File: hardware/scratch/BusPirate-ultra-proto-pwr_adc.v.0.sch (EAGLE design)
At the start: 13 parts, among them IC1 IC_MCP1824_ADJ, Q1 DMMT3906W, Q2 DMMT3906W, U1 IC_OP-AMP_MCP6001

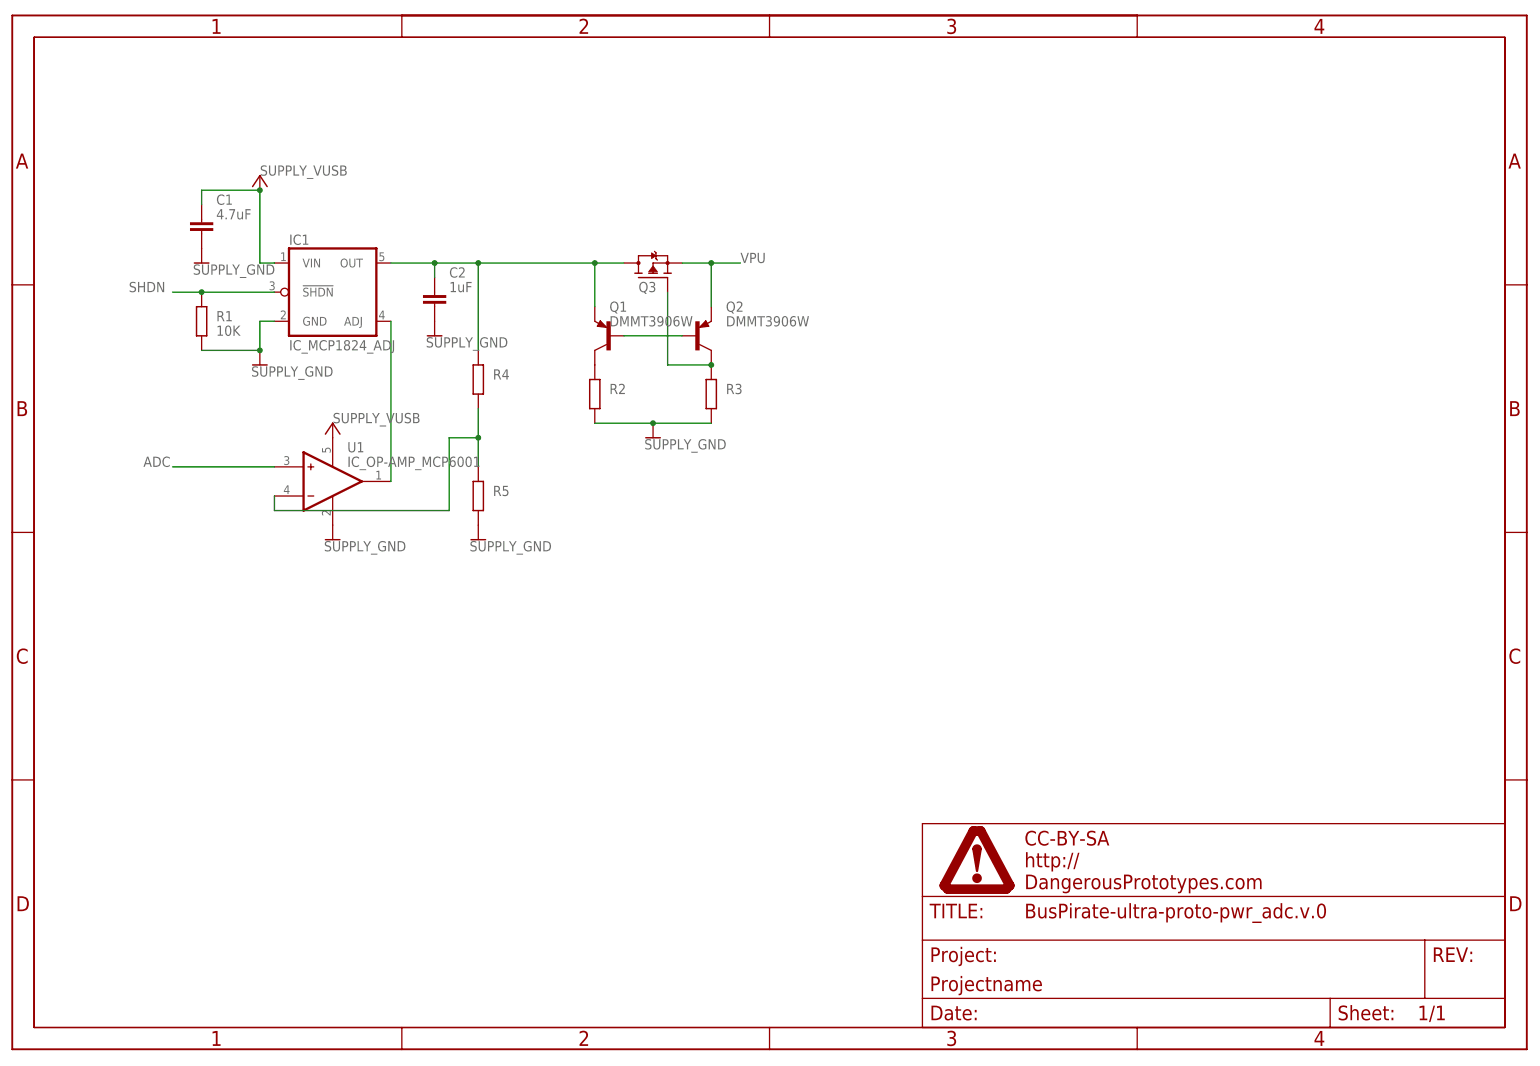
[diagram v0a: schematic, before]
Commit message: initial ADC circuit added
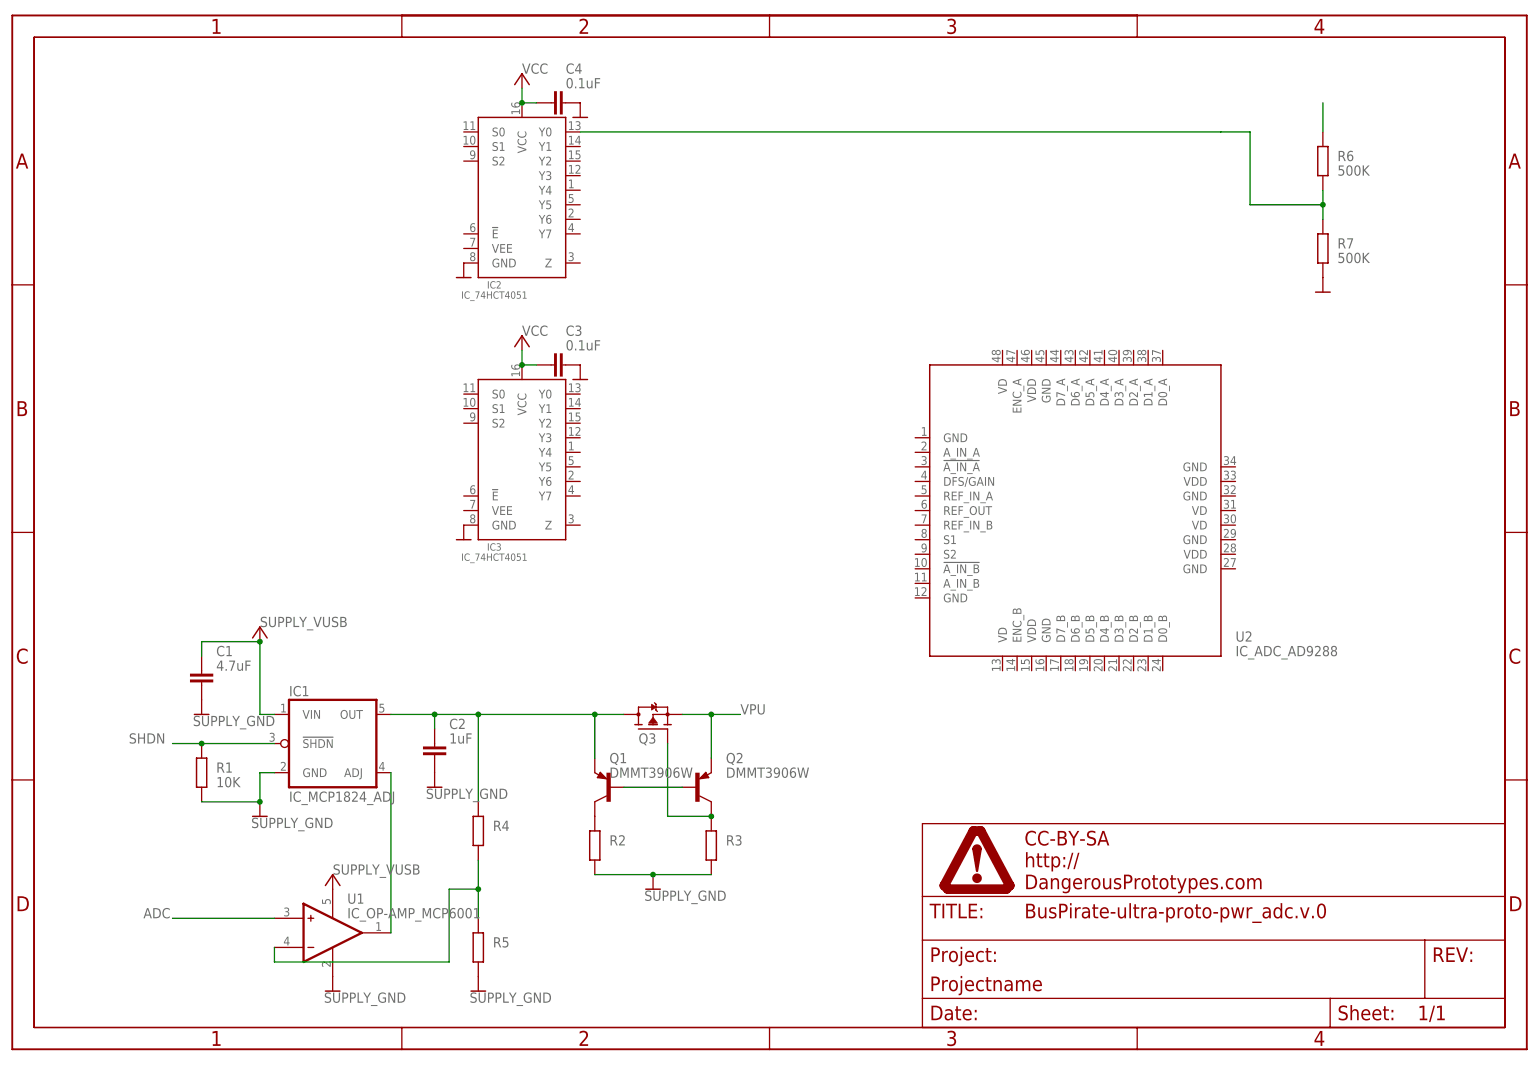
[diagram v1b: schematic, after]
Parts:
- added C3, C4: 0.1uF, dp_devices.v6:CAPACITOR_NPOL-0603
- added IC2, IC3: IC_74HCT4051, dp_devices.v6:IC_74HCT4051
- added R6, R7: 500K, dp_devices.v6:RESISTOR-0603
- added U2: IC_ADC_AD9288, dp_devices.v6:IC_ADC_AD9288
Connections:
- new net N$2: IC2.Y0, R6.1, R7.2
- new net N$8: R6.2
- new net VCC: C3.1, C4.1, IC2.VCC, IC3.VCC
- net GND: now also C3.2, C4.2, IC2.GND, IC3.GND, R7.1
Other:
- moved on the sheet: C1, C2, IC1, Q1, Q2, Q3, R1, R2, R3, R4, R5, U1
